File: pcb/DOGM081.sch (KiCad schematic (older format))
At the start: 4 parts, among them P1 CONN_01X06, U1 EA_DOGMxxx-A

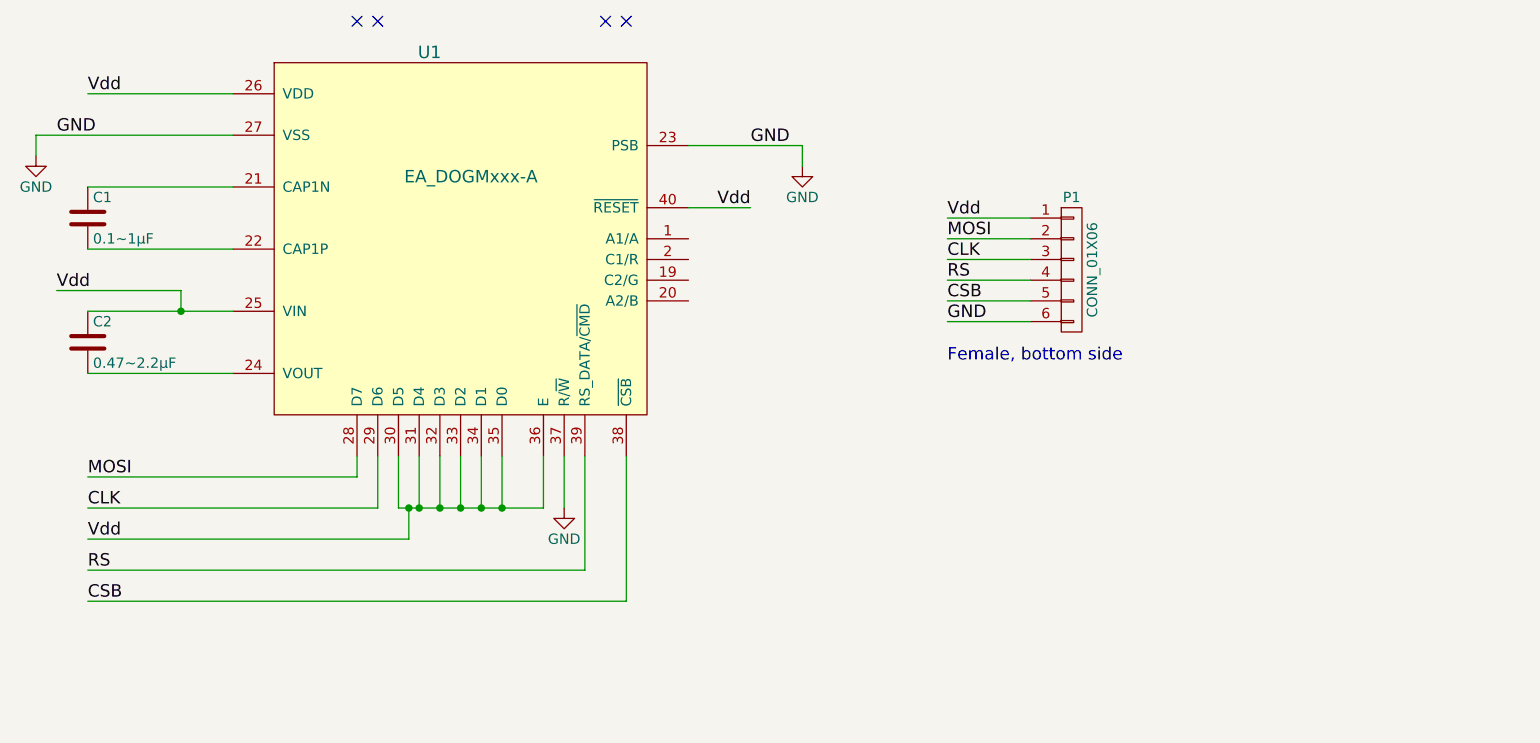
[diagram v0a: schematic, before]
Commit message: Started the revision 2 to support a backlight and a generic connector
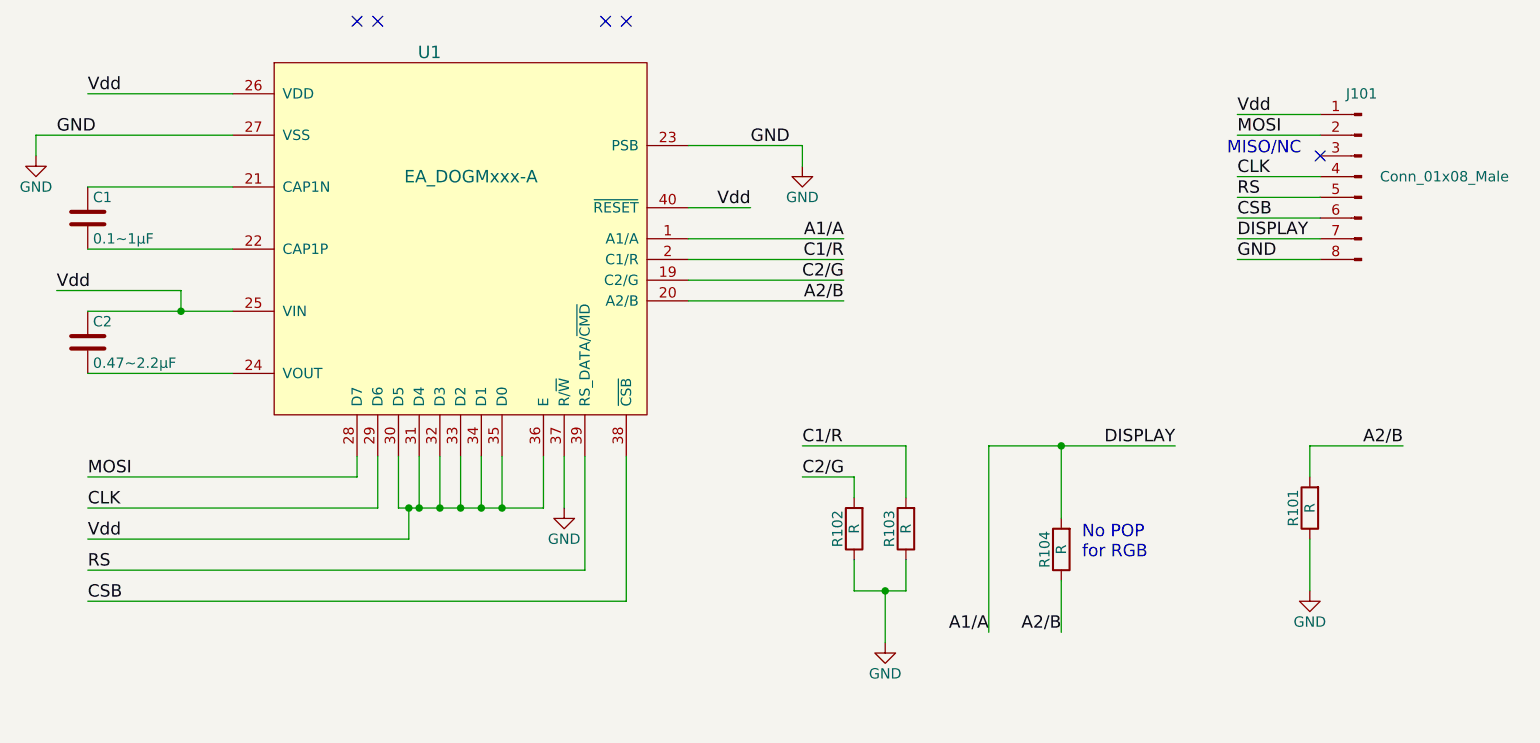
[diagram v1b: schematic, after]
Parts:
- removed P1: CONN_01X06, Socket_Strips:Socket_Strip_Straight_1x06_Pitch2.54mm, symbol CONN_01X06
- added J101: Conn_01x08_Male, symbol Conn_01x08_Male
- added R101, R102, R103, R104: R, symbol R
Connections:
- net CLK: now also J101.4 (Pin_4)
- net CSB: now also J101.6 (Pin_6)
- net GND: now also J101.8 (Pin_8), R101.1, R102.1, R103.1
- net MOSI: now also J101.2 (Pin_2)
- net RS: now also J101.5 (Pin_5)
- net Vdd: now also J101.1 (Pin_1)
- net A1/A: now reaches U1.1 (A1/A)
- net A1/A: now also J101.7 (Pin_7), R104.2
- net C2/G: now reaches U1.19 (C2/G)
- net C2/G: now also R102.2
- net C1/R: now reaches U1.2 (C1/R)
- net C1/R: now also R103.2
- net A2/B: now reaches U1.20 (A2/B)
- net A2/B: now also R101.2, R104.1
- no-connect marks 4 -> 5
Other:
- note added: "MISO/NC"
- note added: "No POP \nfor RGB"
- note removed: "Female, bottom side"
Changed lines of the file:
@@
 	1    0    0    -1
 $EndComp
-Wire Wire Line
-	3450 2650 2750 2650
-Wire Wire Line
-	3450 2950 2750 2950
-Wire Wire Line
-	2750 3250 3450 3250
-Wire Wire Line
-	3450 3550 2750 3550
-Wire Wire Line
-	3200 3250 3200 3150
-Wire Wire Line
-	3200 3150 2600 3150
-Connection ~ 3200 3250
 Text Label 2600 3150 0    60   ~ 0
 Vdd
-Wire Wire Line
-	3450 2200 2750 2200
-Wire Wire Line
-	3450 2400 2500 2400
-Wire Wire Line
-	2500 2400 2500 2500
-$Comp
-L GND #PWR01
+$Comp
+L GND #PWR101
 U 1 1 598B209F
 P 2500 2500
-F 0 "#PWR01" H 2500 2250 50  0001 C CNN
+F 0 "#PWR101" H 2500 2250 50  0001 C CNN
 F 1 "GND" H 2500 2350 50  0000 C CNN
 F 2 "" H 2500 2500 60  0000 C CNN
@@
 	1    0    0    -1
 $EndComp
-Wire Wire Line
-	4050 3950 4050 4050
-Wire Wire Line
-	4050 4050 2750 4050
-Wire Wire Line
-	4150 3950 4150 4200
-Wire Wire Line
-	4150 4200 2750 4200
-Wire Wire Line
-	4250 3950 4250 4200
-Wire Wire Line
-	4250 4200 4950 4200
-Wire Wire Line
-	4950 4200 4950 3950
-Wire Wire Line
-	4350 3950 4350 4200
-Connection ~ 4350 4200
-Wire Wire Line
-	4450 3950 4450 4200
-Connection ~ 4450 4200
-Wire Wire Line
-	4550 3950 4550 4200
-Connection ~ 4550 4200
-Wire Wire Line
-	4650 3950 4650 4200
-Connection ~ 4650 4200
-Wire Wire Line
-	4750 3950 4750 4200
-Connection ~ 4750 4200
-Wire Wire Line
-	4300 4200 4300 4350
-Wire Wire Line
-	4300 4350 2750 4350
-Connection ~ 4300 4200
 Text Label 2750 4350 0    60   ~ 0
 Vdd
 $Comp
-L GND #PWR02
+L GND #PWR103
 U 1 1 598B248A
 P 5050 4200
-F 0 "#PWR02" H 5050 3950 50  0001 C CNN
+F 0 "#PWR103" H 5050 3950 50  0001 C CNN
 F 1 "GND" H 5050 4050 50  0000 C CNN
 F 2 "" H 5050 4200 60  0000 C CNN
@@
 	1    0    0    -1
 $EndComp
-Wire Wire Line
-	5050 3950 5050 4200
-Wire Wire Line
-	5150 3950 5150 4500
-Wire Wire Line
-	5150 4500 2750 4500
-Wire Wire Line
-	5350 3950 5350 4650
-Wire Wire Line
-	5350 4650 2750 4650
-$Comp
-L GND #PWR03
+$Comp
+L GND #PWR102
 U 1 1 598B252B
 P 6200 2550
-F 0 "#PWR03" H 6200 2300 50  0001 C CNN
+F 0 "#PWR102" H 6200 2300 50  0001 C CNN
 F 1 "GND" H 6200 2400 50  0000 C CNN
 F 2 "" H 6200 2550 60  0000 C CNN
@@
 	1    0    0    -1
 $EndComp
-Wire Wire Line
-	5650 2750 5950 2750
-Wire Wire Line
-	6200 2550 6200 2450
-Wire Wire Line
-	6200 2450 5650 2450
 NoConn ~ 4050 1850
 NoConn ~ 4150 1850
@@
 Text Label 2750 4650 0    60   ~ 0
 CSB
-$Comp
-L CONN_01X06 P1
-U 1 1 598B27C6
-P 7500 3050
-F 0 "P1" H 7500 3400 50  0000 C CNN
-F 1 "CONN_01X06" V 7600 3050 50  0000 C CNN
-F 2 "Socket_Strips:Socket_Strip_Straight_1x06_Pitch2.54mm" H 7500 3050 60  0001 C CNN
-F 3 "" H 7500 3050 60  0000 C CNN
-	1    7500 3050
-	1    0    0    -1
-$EndComp
-Wire Wire Line
-	7300 2800 6900 2800
-Wire Wire Line
-	7300 2900 6900 2900
-Wire Wire Line
-	7300 3000 6900 3000
-Wire Wire Line
-	7300 3100 6900 3100
-Wire Wire Line
-	7300 3200 6900 3200
-Wire Wire Line
-	7300 3300 6900 3300
 Text Label 2600 2400 0    60   ~ 0
 GND
 Text Label 5950 2450 0    60   ~ 0
 GND
-Text Label 6900 3300 0    60   ~ 0
+Text Label 8300 3000 0    60   ~ 0
 GND
-Text Label 6900 2800 0    60   ~ 0
+Text Label 8300 2300 0    60   ~ 0
 Vdd
-Text Label 6900 2900 0    60   ~ 0
+Text Label 8300 2400 0    60   ~ 0
 MOSI
-Text Label 6900 3000 0    60   ~ 0
+Text Label 8300 2600 0    60   ~ 0
 CLK
-Text Label 6900 3100 0    60   ~ 0
+Text Label 8300 2700 0    60   ~ 0
 RS
-Text Label 6900 3200 0    60   ~ 0
+Text Label 8300 2800 0    60   ~ 0
 CSB
-Text Notes 6900 3500 0    60   ~ 0
-Female, bottom side
+$Comp
+L R R103
+U 1 1 5A6B86C1
+P 6700 4300
+F 0 "R103" V 6780 4300 50  0000 C CNN
+F 1 "R" V 6700 4300 50  0000 C CNN
+F 2 "" V 6630 4300 50  0001 C CNN
+F 3 "" H 6700 4300 50  0001 C CNN
+	1    6700 4300
+	-1   0    0    1
+$EndComp
+$Comp
+L R R102
+U 1 1 5A6B87AF
+P 6450 4300
+F 0 "R102" V 6530 4300 50  0000 C CNN
+F 1 "R" V 6450 4300 50  0000 C CNN
+F 2 "" V 6380 4300 50  0001 C CNN
+F 3 "" H 6450 4300 50  0001 C CNN
+	1    6450 4300
+	-1   0    0    1
+$EndComp
+Text Label 6400 2900 2    60   ~ 0
+A1/A
+Text Label 6400 3200 2    60   ~ 0
+A2/B
+Text Label 6400 3000 2    60   ~ 0
+C1/R
+Text Label 6400 3100 2    60   ~ 0
+C2/G
+Text Label 8000 3900 2    60   ~ 0
+DISPLAY
+$Comp
+L GND #PWR105
+U 1 1 5A6B8C02
+P 6600 4850
+F 0 "#PWR105" H 6600 4600 50  0001 C CNN
+F 1 "GND" H 6600 4700 50  0000 C CNN
+F 2 "" H 6600 4850 60  0000 C CNN
+F 3 "" H 6600 4850 60  0000 C CNN
+	1    6600 4850
+	1    0    0    -1
+$EndComp
+Text Label 6200 3900 0    60   ~ 0
+C1/R
+Text Label 6200 4050 0    60   ~ 0
+C2/G
+Wire Wire Line
+	3450 2650 2750 2650
+Wire Wire Line
+	3450 2950 2750 2950
+Wire Wire Line
+	2750 3250 3450 3250
+Wire Wire Line
+	3450 3550 2750 3550
+Wire Wire Line
+	3200 3250 3200 3150
+Wire Wire Line
+	3200 3150 2600 3150
+Connection ~ 3200 3250
+Wire Wire Line
+	3450 2200 2750 2200
+Wire Wire Line
+	3450 2400 2500 2400
+Wire Wire Line
+	2500 2400 2500 2500
+Wire Wire Line
+	4050 3950 4050 4050
+Wire Wire Line
+	4050 4050 2750 4050
+Wire Wire Line
+	4150 3950 4150 4200
+Wire Wire Line
+	4150 4200 2750 4200
+Wire Wire Line
+	4250 3950 4250 4200
+Wire Wire Line
+	4250 4200 4950 4200
+Wire Wire Line
+	4950 4200 4950 3950
+Wire Wire Line
+	4350 3950 4350 4200
+Connection ~ 4350 4200
+Wire Wire Line
+	4450 3950 4450 4200
+Connection ~ 4450 4200
+Wire Wire Line
+	4550 3950 4550 4200
+Connection ~ 4550 4200
+Wire Wire Line
+	4650 3950 4650 4200
+Connection ~ 4650 4200
+Wire Wire Line
+	4750 3950 4750 4200
+Connection ~ 4750 4200
+Wire Wire Line
+	4300 4200 4300 4350
+Wire Wire Line
+	4300 4350 2750 4350
+Connection ~ 4300 4200
+Wire Wire Line
+	5050 3950 5050 4200
+Wire Wire Line
+	5150 3950 5150 4500
+Wire Wire Line
+	5150 4500 2750 4500
+Wire Wire Line
+	5350 3950 5350 4650
+Wire Wire Line
+	5350 4650 2750 4650
+Wire Wire Line
+	5650 2750 5950 2750
+Wire Wire Line
+	6200 2550 6200 2450
+Wire Wire Line
+	6200 2450 5650 2450
+Wire Wire Line
+	8700 2300 8300 2300
+Wire Wire Line
+	8700 2400 8300 2400
+Wire Wire Line
+	8700 2600 8300 2600
+Wire Wire Line
+	8700 2700 8300 2700
+Wire Wire Line
+	8700 2800 8300 2800
+Wire Wire Line
+	5650 2900 6400 2900
+Wire Wire Line
+	6400 3200 5650 3200
+Wire Wire Line
+	5650 3000 6400 3000
+Wire Wire Line
+	5650 3100 6400 3100
+Wire Wire Line
+	7100 3900 8000 3900
+Wire Wire Line
+	6700 4600 6700 4450
+Wire Wire Line
+	6450 4450 6450 4600
+Wire Wire Line
+	6450 4600 6700 4600
+Wire Wire Line
+	6600 4600 6600 4850
+Connection ~ 6600 4600
+Wire Wire Line
+	6450 4150 6450 4050
+Wire Wire Line
+	6450 4050 6200 4050
+Wire Wire Line
+	6700 4150 6700 3900
+Wire Wire Line
+	6700 3900 6200 3900
+Wire Wire Line
+	7100 3900 7100 4800
+Text Label 7100 4800 2    60   ~ 0
+A1/A
+Wire Wire Line
+	7450 3900 7450 4250
+Connection ~ 7450 3900
+$Comp
+L R R104
+U 1 1 5A6B8EF0
+P 7450 4400
+F 0 "R104" V 7530 4400 50  0000 C CNN
+F 1 "R" V 7450 4400 50  0000 C CNN
+F 2 "" V 7380 4400 50  0001 C CNN
+F 3 "" H 7450 4400 50  0001 C CNN
+	1    7450 4400
+	-1   0    0    1
+$EndComp
+Wire Wire Line
+	7450 4550 7450 4800
+Text Label 7450 4800 2    60   ~ 0
+A2/B
+$Comp
+L R R101
+U 1 1 5A6B9127
+P 8650 4200
+F 0 "R101" V 8730 4200 50  0000 C CNN
+F 1 "R" V 8650 4200 50  0000 C CNN
+F 2 "" V 8580 4200 50  0001 C CNN
+F 3 "" H 8650 4200 50  0001 C CNN
+	1    8650 4200
+	-1   0    0    1
+$EndComp
+Wire Wire Line
+	8650 4050 8650 3900
+Wire Wire Line
+	8650 3900 9100 3900
+Text Label 9100 3900 2    60   ~ 0
+A2/B
+Wire Wire Line
+	8650 4600 8650 4350
+$Comp
+L GND #PWR104
+U 1 1 5A6B939C
+P 8650 4600
+F 0 "#PWR104" H 8650 4350 50  0001 C CNN
+F 1 "GND" H 8650 4450 50  0000 C CNN
+F 2 "" H 8650 4600 60  0000 C CNN
+F 3 "" H 8650 4600 60  0000 C CNN
+	1    8650 4600
+	1    0    0    -1
+$EndComp
+Text Notes 7550 4450 0    60   ~ 0
+No POP \nfor RGB
+$Comp
+L Conn_01x08_Male J101
+U 1 1 5A6B955F
+P 8900 2600
+F 0 "J101" H 8900 3000 50  0000 C CNN
+F 1 "Conn_01x08_Male" H 8500 2600 50  0000 C CNN
+F 2 "" H 8900 2600 50  0001 C CNN
+F 3 "" H 8900 2600 50  0001 C CNN
+	1    8900 2600
+	-1   0    0    -1
+$EndComp
+Wire Wire Line
+	8700 2900 8300 2900
+Wire Wire Line
+	8700 3000 8300 3000
+Text Label 8300 2900 0    60   ~ 0
+DISPLAY
+NoConn ~ 8700 2500
+Text Notes 8250 2500 0    60   ~ 0
+MISO/NC
 $EndSCHEMATC

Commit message: Complted the Rev2 layout and sent to OSHPark. Feature for back-light
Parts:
- removed J101: Conn_01x08_Male, symbol Conn_01x08_Male
- added J101: Conn_01x10_Male, Pin_Headers:Pin_Header_Straight_1x10_Pitch2.54mm, symbol Conn_01x10_Male
- added Q101: IRLML2502GTRPBF, TO_SOT_Packages_SMD:SOT-23, symbol Q_NMOS_GSD
- added R105: R, Resistors_SMD:R_0805_HandSoldering, symbol R
- R101, R102, R103, R104: footprint (none) -> Resistors_SMD:R_0805_HandSoldering
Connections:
- net CLK: now also J101.4 (Pin_4)
- net CSB: now also J101.5 (Pin_5)
- net GND: now also J101.10 (Pin_10), R105.1
- net MOSI: now also J101.2 (Pin_2)
- net RS: now also J101.6 (Pin_6)
- net Vdd: now also J101.1 (Pin_1), Q101.3 (D)
- net A1/A renamed A1_A
- net A1_A: now also Q101.2 (S)
- net A2/B renamed A2_B
- net C1/R renamed C1_R
- net C2/G renamed C2_G
- new net BACKLIGHT: J101.8 (Pin_8), Q101.1 (G), R105.2
- no-connect marks 5 -> 3
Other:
- note added: "NC"
- note added: "No POP \nfor RGB!"
- note added: "Only \nfor B!"
- note added: "~RESET~/NC"
- note removed: "No POP \nfor RGB"
- moved on the sheet: R101, R104
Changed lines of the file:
@@
 Vdd
 $Comp
-L GND #PWR101
+L GND #PWR01
 U 1 1 598B209F
 P 2500 2500
-F 0 "#PWR101" H 2500 2250 50  0001 C CNN
+F 0 "#PWR01" H 2500 2250 50  0001 C CNN
 F 1 "GND" H 2500 2350 50  0000 C CNN
 F 2 "" H 2500 2500 60  0000 C CNN
@@
 Vdd
 $Comp
-L GND #PWR103
+L GND #PWR02
 U 1 1 598B248A
 P 5050 4200
-F 0 "#PWR103" H 5050 3950 50  0001 C CNN
+F 0 "#PWR02" H 5050 3950 50  0001 C CNN
 F 1 "GND" H 5050 4050 50  0000 C CNN
 F 2 "" H 5050 4200 60  0000 C CNN
@@
 $EndComp
 $Comp
-L GND #PWR102
+L GND #PWR03
 U 1 1 598B252B
 P 6200 2550
-F 0 "#PWR102" H 6200 2300 50  0001 C CNN
+F 0 "#PWR03" H 6200 2300 50  0001 C CNN
 F 1 "GND" H 6200 2400 50  0000 C CNN
 F 2 "" H 6200 2550 60  0000 C CNN
@@
 	1    0    0    -1
 $EndComp
-NoConn ~ 4050 1850
-NoConn ~ 4150 1850
-NoConn ~ 5250 1850
-NoConn ~ 5350 1850
 Text Label 2750 4050 0    60   ~ 0
 MOSI
@@
 Text Label 5950 2450 0    60   ~ 0
 GND
-Text Label 8300 3000 0    60   ~ 0
-GND
 Text Label 8300 2300 0    60   ~ 0
 Vdd
@@
 Text Label 8300 2600 0    60   ~ 0
 CLK
+Text Label 8300 2800 0    60   ~ 0
+RS
 Text Label 8300 2700 0    60   ~ 0
-RS
-Text Label 8300 2800 0    60   ~ 0
 CSB
 $Comp
@@
 F 0 "R103" V 6780 4300 50  0000 C CNN
 F 1 "R" V 6700 4300 50  0000 C CNN
-F 2 "" V 6630 4300 50  0001 C CNN
+F 2 "Resistors_SMD:R_0805_HandSoldering" V 6630 4300 50  0001 C CNN
 F 3 "" H 6700 4300 50  0001 C CNN
 	1    6700 4300
@@
 F 0 "R102" V 6530 4300 50  0000 C CNN
 F 1 "R" V 6450 4300 50  0000 C CNN
-F 2 "" V 6380 4300 50  0001 C CNN
+F 2 "Resistors_SMD:R_0805_HandSoldering" V 6380 4300 50  0001 C CNN
 F 3 "" H 6450 4300 50  0001 C CNN
 	1    6450 4300
@@
 $EndComp
 Text Label 6400 2900 2    60   ~ 0
-A1/A
+A1_A
 Text Label 6400 3200 2    60   ~ 0
-A2/B
+A2_B
 Text Label 6400 3000 2    60   ~ 0
-C1/R
+C1_R
 Text Label 6400 3100 2    60   ~ 0
-C2/G
-Text Label 8000 3900 2    60   ~ 0
-DISPLAY
-$Comp
-L GND #PWR105
+C2_G
+Text Label 9200 3750 2    60   ~ 0
+BACKLIGHT
+$Comp
+L GND #PWR04
 U 1 1 5A6B8C02
 P 6600 4850
-F 0 "#PWR105" H 6600 4600 50  0001 C CNN
+F 0 "#PWR04" H 6600 4600 50  0001 C CNN
 F 1 "GND" H 6600 4700 50  0000 C CNN
 F 2 "" H 6600 4850 60  0000 C CNN
@@
 	1    0    0    -1
 $EndComp
-Text Label 6200 3900 0    60   ~ 0
-C1/R
-Text Label 6200 4050 0    60   ~ 0
-C2/G
 Wire Wire Line
 	3450 2650 2750 2650
@@
 	5650 3100 6400 3100
 Wire Wire Line
-	7100 3900 8000 3900
+	7600 4300 7900 4300
 Wire Wire Line
 	6700 4600 6700 4450
@@
 	6700 3900 6200 3900
 Wire Wire Line
-	7100 3900 7100 4800
-Text Label 7100 4800 2    60   ~ 0
-A1/A
-Wire Wire Line
-	7450 3900 7450 4250
-Connection ~ 7450 3900
+	7600 4300 7600 5200
 $Comp
 L R R104
 U 1 1 5A6B8EF0
-P 7450 4400
-F 0 "R104" V 7530 4400 50  0000 C CNN
-F 1 "R" V 7450 4400 50  0000 C CNN
-F 2 "" V 7380 4400 50  0001 C CNN
-F 3 "" H 7450 4400 50  0001 C CNN
-	1    7450 4400
-	-1   0    0    1
-$EndComp
-Wire Wire Line
-	7450 4550 7450 4800
-Text Label 7450 4800 2    60   ~ 0
-A2/B
+P 7900 4600
+F 0 "R104" V 7980 4600 50  0000 C CNN
+F 1 "R" V 7900 4600 50  0000 C CNN
+F 2 "Resistors_SMD:R_0805_HandSoldering" V 7830 4600 50  0001 C CNN
+F 3 "" H 7900 4600 50  0001 C CNN
+	1    7900 4600
+	-1   0    0    1
+$EndComp
 $Comp
 L R R101
 U 1 1 5A6B9127
-P 8650 4200
-F 0 "R101" V 8730 4200 50  0000 C CNN
-F 1 "R" V 8650 4200 50  0000 C CNN
-F 2 "" V 8580 4200 50  0001 C CNN
-F 3 "" H 8650 4200 50  0001 C CNN
-	1    8650 4200
-	-1   0    0    1
-$EndComp
-Wire Wire Line
-	8650 4050 8650 3900
-Wire Wire Line
-	8650 3900 9100 3900
-Text Label 9100 3900 2    60   ~ 0
-A2/B
-Wire Wire Line
-	8650 4600 8650 4350
-$Comp
-L GND #PWR104
+P 6050 4650
+F 0 "R101" V 6130 4650 50  0000 C CNN
+F 1 "R" V 6050 4650 50  0000 C CNN
+F 2 "Resistors_SMD:R_0805_HandSoldering" V 5980 4650 50  0001 C CNN
+F 3 "" H 6050 4650 50  0001 C CNN
+	1    6050 4650
+	-1   0    0    1
+$EndComp
+Wire Wire Line
+	6050 4500 6050 4350
+Wire Wire Line
+	6050 4350 5800 4350
+Wire Wire Line
+	6050 5050 6050 4800
+$Comp
+L GND #PWR05
 U 1 1 5A6B939C
-P 8650 4600
-F 0 "#PWR104" H 8650 4350 50  0001 C CNN
-F 1 "GND" H 8650 4450 50  0000 C CNN
-F 2 "" H 8650 4600 60  0000 C CNN
-F 3 "" H 8650 4600 60  0000 C CNN
-	1    8650 4600
-	1    0    0    -1
-$EndComp
-Text Notes 7550 4450 0    60   ~ 0
-No POP \nfor RGB
-$Comp
-L Conn_01x08_Male J101
-U 1 1 5A6B955F
-P 8900 2600
-F 0 "J101" H 8900 3000 50  0000 C CNN
-F 1 "Conn_01x08_Male" H 8500 2600 50  0000 C CNN
-F 2 "" H 8900 2600 50  0001 C CNN
-F 3 "" H 8900 2600 50  0001 C CNN
-	1    8900 2600
-	-1   0    0    -1
-$EndComp
-Wire Wire Line
-	8700 2900 8300 2900
+P 6050 5050
+F 0 "#PWR05" H 6050 4800 50  0001 C CNN
+F 1 "GND" H 6050 4900 50  0000 C CNN
+F 2 "" H 6050 5050 60  0000 C CNN
+F 3 "" H 6050 5050 60  0000 C CNN
+	1    6050 5050
+	1    0    0    -1
+$EndComp
+Text Notes 8000 4700 0    60   ~ 0
+No POP \nfor RGB!
 Wire Wire Line
 	8700 3000 8300 3000
-Text Label 8300 2900 0    60   ~ 0
-DISPLAY
+Text Label 8300 3000 0    60   ~ 0
+BACKLIGHT
 NoConn ~ 8700 2500
 Text Notes 8250 2500 0    60   ~ 0
 MISO/NC
+$Comp
+L Q_NMOS_GSD Q101
+U 1 1 5A6C9B9E
+P 8000 3750
+F 0 "Q101" H 8200 3800 50  0000 L CNN
+F 1 "IRLML2502GTRPBF" H 8200 3700 50  0000 L CNN
+F 2 "TO_SOT_Packages_SMD:SOT-23" H 8200 3850 50  0001 C CNN
+F 3 "https://www.infineon.com/dgdl/irlml2502gpbf.pdf?fileId=5546d462533600a401535667fb882604" H 8000 3750 50  0001 C CNN
+F 4 "IRLML2502GTRPBF" H 8000 3750 60  0001 C CNN "MPN"
+F 5 "Value" H 8000 3750 60  0001 C CNN "Link"
+F 6 "Value" H 8000 3750 60  0001 C CNN "Comp_Name"
+	1    8000 3750
+	-1   0    0    -1
+$EndComp
+Wire Wire Line
+	7900 3550 7900 3400
+Wire Wire Line
+	7900 3400 7600 3400
+Text Label 7600 3400 0    60   ~ 0
+Vdd
+$Comp
+L R R105
+U 1 1 5A6C9E79
+P 8700 4100
+F 0 "R105" V 8780 4100 50  0000 C CNN
+F 1 "R" V 8700 4100 50  0000 C CNN
+F 2 "Resistors_SMD:R_0805_HandSoldering" V 8630 4100 50  0001 C CNN
+F 3 "" H 8700 4100 50  0001 C CNN
+	1    8700 4100
+	-1   0    0    1
+$EndComp
+Wire Wire Line
+	8700 4250 8700 4750
+$Comp
+L GND #PWR06
+U 1 1 5A6C9F7F
+P 8700 4750
+F 0 "#PWR06" H 8700 4500 50  0001 C CNN
+F 1 "GND" H 8700 4600 50  0000 C CNN
+F 2 "" H 8700 4750 60  0000 C CNN
+F 3 "" H 8700 4750 60  0000 C CNN
+	1    8700 4750
+	1    0    0    -1
+$EndComp
+Wire Wire Line
+	7900 3950 7900 4450
+Connection ~ 7900 4300
+Wire Wire Line
+	7900 4750 7900 5200
+Text Notes 6100 4750 0    60   ~ 0
+Only \nfor B!
+Wire Wire Line
+	8200 3750 9200 3750
+Wire Wire Line
+	8700 3750 8700 3950
+Connection ~ 8700 3750
+Text Label 5800 4350 0    60   ~ 0
+A2_B
+Text Label 6200 3900 0    60   ~ 0
+C1_R
+Text Label 6200 4050 0    60   ~ 0
+C2_G
+Text Label 7600 5200 2    60   ~ 0
+A1_A
+Text Label 7900 5200 2    60   ~ 0
+A2_B
+$Comp
+L Conn_01x10_Male J101
+U 1 1 5A6CAC2E
+P 8900 2700
+F 0 "J101" H 8900 3200 50  0000 C CNN
+F 1 "Conn_01x10_Male" H 8900 2100 50  0000 C CNN
+F 2 "Pin_Headers:Pin_Header_Straight_1x10_Pitch2.54mm" H 8900 2700 50  0001 C CNN
+F 3 "" H 8900 2700 50  0001 C CNN
+	1    8900 2700
+	-1   0    0    -1
+$EndComp
+Wire Wire Line
+	8700 3200 8300 3200
+Text Label 8300 3200 0    60   ~ 0
+GND
+NoConn ~ 8700 2900
+NoConn ~ 8700 3100
+Text Notes 8200 2900 0    60   ~ 0
+~RESET~/NC
+Text Notes 8250 3100 0    60   ~ 0
+NC
 $EndSCHEMATC
